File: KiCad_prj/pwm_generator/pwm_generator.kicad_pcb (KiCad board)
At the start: 2 copper layers, 100 x 46 mm, 89 parts, among them J1 MLW20A, J2 MLW10A, U1 LM2664 / LM2665, U10 OPA365xxDBV, U11 TLV3501AIDBV, U12 OPA365xxDBV, U13 TLV3501AIDBV, U2 74HC14, U3 TL431DBZ, U4 OPA365xxDBV, U5 TLV3501AIDBV, U6 OPA197xDBV, U7 OPA197xDBV, U8 OPA197xDBV, U9 OPA197xDBV

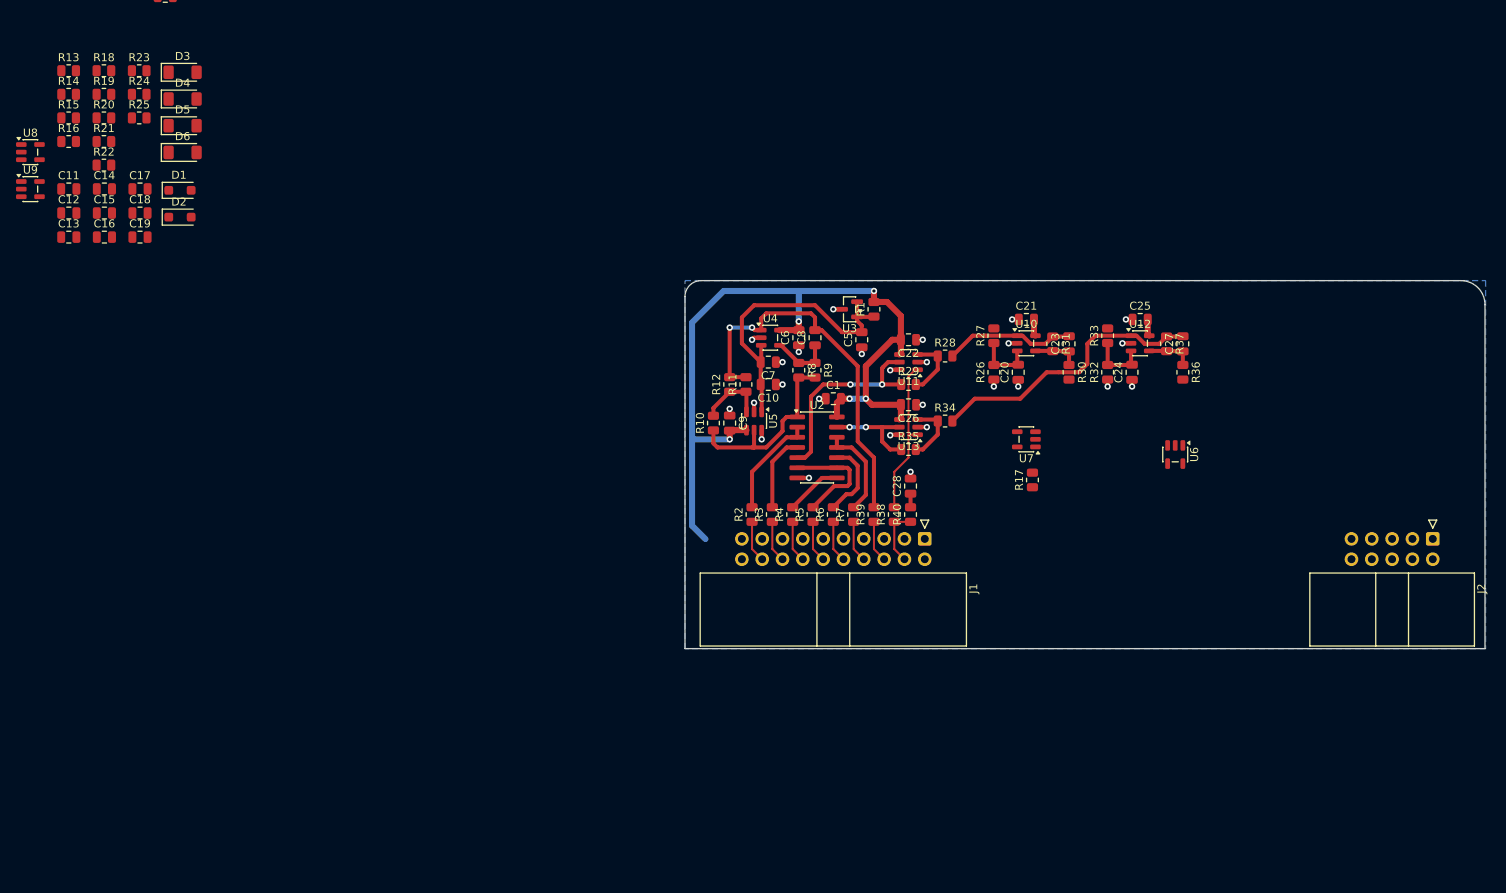
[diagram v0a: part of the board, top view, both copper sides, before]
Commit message: Upravaa DPS pwm generatoru
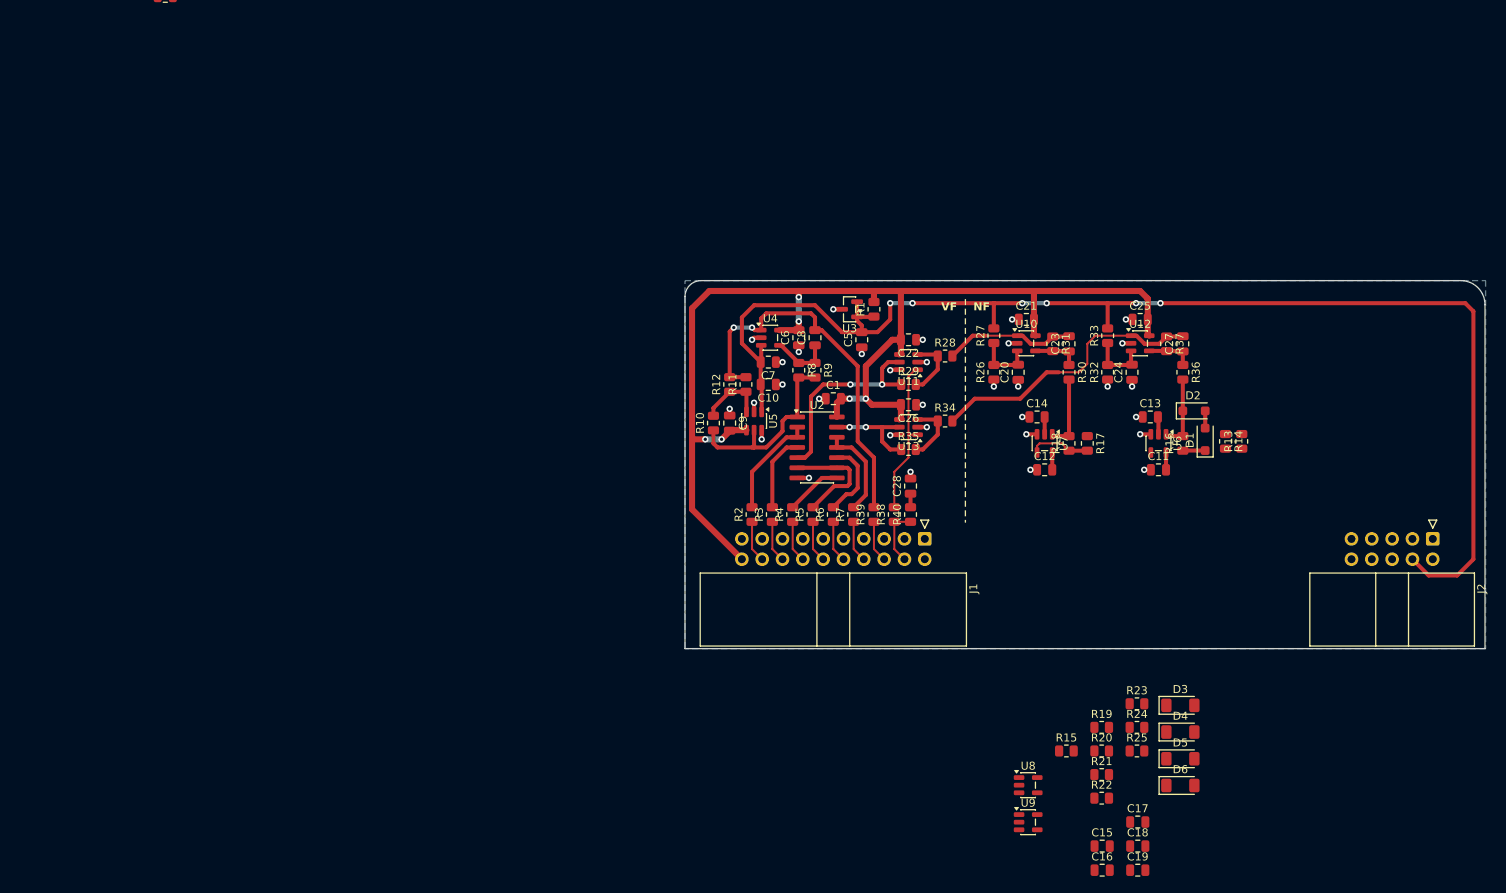
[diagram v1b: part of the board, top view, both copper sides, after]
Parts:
- moved R13 153.8 mm to (174.6, 104.1), turned to 90 degrees
- moved R14 151.0 mm to (172.6, 104.1), turned to -90 degrees
- moved C17 147.7 mm to (161.6, 151.7)
- moved C18 147.7 mm to (161.6, 154.7)
- moved C19 147.7 mm to (161.6, 157.7)
- moved R23 147.7 mm to (161.5, 136.9)
- moved R24 147.7 mm to (161.5, 139.8)
- moved R25 147.7 mm to (161.5, 142.8)
- moved C15 147.7 mm to (157.1, 154.7)
- moved C16 147.7 mm to (157.1, 157.7)
- moved D3 147.7 mm to (166.9, 137.1)
- moved D4 147.7 mm to (166.9, 140.4)
- moved D5 147.7 mm to (166.9, 143.8)
- moved D6 147.7 mm to (166.9, 147.1)
- moved R15 147.7 mm to (152.7, 142.8)
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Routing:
- net /U_{REF}: track 38.2 -> 164.3 mm, vias 0 -> 6
- net +5V: track 104.0 -> 153.0 mm, vias 5 -> 6
- net /PWM_CHA/SIGNAL_AC: track 0.00 -> 9.26 mm
- net /PWM_CHB/SIGNAL_AC: track 0.00 -> 9.26 mm
- net Net-(U7--): track 0.00 -> 7.61 mm
- net GND: track 25.5 -> 31.6 mm, vias 26 -> 32
- net -5V: track 0.00 -> 4.36 mm
- net Net-(D1-K): track 0.00 -> 2.80 mm
- net Net-(D1-A): track 0.00 -> 2.16 mm
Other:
- board text added: "NF"
- board text added: "VF"

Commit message: Dokoncene trasy na DPS pwm_generator
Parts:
- added C29: 100n, Capacitor_SMD:C_0805_2012Metric, F.Cu at (176.6, 91.9)
- added C30: 100n, Capacitor_SMD:C_0805_2012Metric, F.Cu at (142.6, 88.1)
- added C31: 100n, Capacitor_SMD:C_0805_2012Metric, F.Cu at (156.8, 88.1)
- added C32: 100n, Capacitor_SMD:C_0805_2012Metric, F.Cu at (109.6, 113.2)
- added C33: 100n, Capacitor_SMD:C_0805_2012Metric, F.Cu at (137.5, 113.2)
- moved C4 120.3 mm to (144.9, 107.4), turned to -90 degrees
- moved C3 119.9 mm to (141.6, 109.2)
- moved C2 117.8 mm to (138.3, 107.4), turned to -90 degrees
- moved U1 110.3 mm to (141.6, 106.4), turned to 180 degrees
- moved U3 47.7 mm to (173.1, 92.4), turned to -90 degrees
- moved R1 47.1 mm to (175.7, 89.1), turned to 0 degrees
- moved C19 45.7 mm to (148.9, 113.7)
- moved C5 44.5 mm to (171.5, 89.1), turned to 180 degrees
- moved C16 44.4 mm to (163.2, 113.7)
- moved R15 38.7 mm to (170.0, 108.2), turned to 90 degrees
- moved C18 36.3 mm to (150.0, 120.3)
- moved D4 35.9 mm to (142.3, 114.3), turned to 90 degrees
- moved C17 35.5 mm to (169.3, 117.0), turned to 90 degrees
- moved C15 35.0 mm to (164.2, 120.3)
- moved U9 34.7 mm to (150.0, 117.0), turned to -90 degrees
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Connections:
- J2 pad 10: /Wave Shaper/COMPENSATION_NEG -> /Wave Shaper/INPUT_SIGNAL
- J2 pad 2: /Wave Shaper/ACDC -> /U_{REF}
- J2 pad 4: /U_{REF} -> /Wave Shaper/ACDC
- J2 pad 6: /Wave Shaper/INPUT_SIGNAL -> /Wave Shaper/COMPENSATION_POS
- J2 pad 8: /Wave Shaper/COMPENSATION_POS -> /Wave Shaper/COMPENSATION_NEG
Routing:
- net +5V: track 153.0 -> 345.4 mm, vias 6 -> 16
- net -5V: track 4.36 -> 65.4 mm, vias 0 -> 4
- net /Wave Shaper/COMPENSATION_POS: track 0.00 -> 41.6 mm
- net /U_{REF}: track 164.3 -> 125.7 mm, vias 6 -> 0
- net /Wave Shaper/COMPENSATION_NEG: track 0.00 -> 28.0 mm
- net Net-(D5-A): track 0.00 -> 21.6 mm, vias 0 -> 2
- net /Wave Shaper/ACDC: track 0.00 -> 18.9 mm
- net /PWM_CHB/SIGNAL_AC: track 9.26 -> 26.3 mm
- net GND: track 31.6 -> 47.2 mm, vias 32 -> 47
- net Net-(D5-K): track 0.00 -> 11.9 mm
- net Net-(D3-A): track 0.00 -> 11.8 mm
- net Net-(C17-Pad2): track 0.00 -> 11.6 mm
- net /Wave Shaper/INPUT_SIGNAL: track 0.00 -> 10.1 mm
- net Net-(U8--): track 0.00 -> 9.32 mm
- net Net-(D1-K): track 2.80 -> 9.34 mm
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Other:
- board size 100 x 46 mm -> 90 x 46 mm
- board text removed: "NF"
- board text removed: "VF"

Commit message: Pruchozi kontrola DRC
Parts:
- moved C2 0.25 mm to (141.6, 109.4)
- renumbered C2 to C1, C7 to C10, C9 to C11, C6 to C12, C8 to C13, C10 to C14, C18 to C17, C19 to C18, C17 to C19, C3 to C2, C11 to C20, C13 to C21, C12 to C22, C14 to C23, C30 to C24, C20 to C25, C21 to C26, C23 to C27, C22 to C28, C31 to C29, C4 to C3, C24 to C30, C25 to C31, C27 to C32, C26 to C33, C29 to C4, C1 to C6, C28 to C7, C32 to C8, C33 to C9, D3 to D1, D4 to D2, D5 to D3, D6 to D4, D1 to D5, D2 to D6, J2 to J1, J1 to J2, R40 to R10, R8 to R11, R9 to R12, R10 to R13, R11 to R14, R12 to R15, R22 to R16, R24 to R17, R23 to R18, R20 to R19, R21 to R20, R25 to R21, R13 to R22, R14 to R23, R15 to R24, R19 to R25, R16 to R26, R17 to R27, R18 to R28, R27 to R29, R26 to R31, R31 to R32, R28 to R33, R29 to R34, R33 to R35, R32 to R37, R37 to R38, R34 to R39, R35 to R40, R39 to R8, R38 to R9, U3 to U2, U2 to U3, U5 to U4, U4 to U5, U8 to U6, U9 to U7, U6 to U8, U7 to U9
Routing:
- net Net-(D5-K): track 9.34 -> 14.7 mm
- net +5V: track 345.4 -> 347.9 mm
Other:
- board text added: "${TITLE} rev. ${REVISION}"
- board text added: "NF"
- board text added: "VF"

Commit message: Uprava DPS generatoru - popisky
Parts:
- added D7: LED, LED_SMD:LED_0805_2012Metric, F.Cu at (182.2, 91.9)
- added R41: 560R, Resistor_SMD:R_0805_2012Metric, F.Cu at (179.4, 90.9)
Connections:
- net /SAMP renamed /TRIG
- net /Triangle Wave Generator/~{SAMPLING} renamed /Triangle Wave Generator/~{TRIGGER}
- net /~{SAMP} renamed /~{TRIG}
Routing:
- net +5V: track 347.9 -> 306.1 mm
- net Net-(D7-A): track 0.00 -> 1.91 mm
- net GND: track 47.2 -> 48.1 mm, vias 47 -> 48
- added copper zone on F.Cu, net +5V
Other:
- board text added: "5V"
- board text added: "A"
- board text added: "AC"
- board text added: "B"
- board text added: "CN"
- board text added: "CP"
- board text added: "DC"
- board text added: "G"
- board text added: "IN"
- board text added: "POWER"
- board text added: "R"
- board text added: "TI"
- board text added: "TO"
- board text added: "TR"
- board text added: "~{A}"
- board text added: "~{B}"
- board text added: "~{TR}"

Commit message: Pridany testpointy a jlcpcb bom reference
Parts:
- added C34: 100n, Capacitor_SMD:C_0805_2012Metric, F.Cu at (174.6, 104.3)
- added R42: 1k, Resistor_SMD:R_0805_2012Metric, F.Cu at (176.6, 107.9)
- added TP1: TestPoint, TestPoint:TestPoint_Loop_D1.80mm_Drill1.0mm_Beaded, F.Cu at (130.4, 107.9)
- added TP2: TestPoint, TestPoint:TestPoint_Loop_D1.80mm_Drill1.0mm_Beaded, F.Cu at (129.4, 97.0)
- added TP3: TestPoint, TestPoint:TestPoint_Loop_D1.80mm_Drill1.0mm_Beaded, F.Cu at (128.7, 102.3)
- added TP4: TestPoint, TestPoint:TestPoint_Loop_D1.80mm_Drill1.0mm_Beaded, F.Cu at (190.9, 86.8)
- added TP5: TestPoint, TestPoint:TestPoint_Loop_D1.80mm_Drill1.0mm_Beaded, F.Cu at (178.5, 86.8)
- added TP6: TestPoint, TestPoint:TestPoint_Loop_D1.80mm_Drill1.0mm_Beaded, F.Cu at (172.4, 113.0)
- added TP7: TestPoint, TestPoint:TestPoint_Loop_D1.80mm_Drill1.0mm_Beaded, F.Cu at (141.1, 93.4)
- added TP8: TestPoint, TestPoint:TestPoint_Loop_D1.80mm_Drill1.0mm_Beaded, F.Cu at (141.1, 101.6)
- added TP9: TestPoint, TestPoint:TestPoint_Loop_D1.80mm_Drill1.0mm_Beaded, F.Cu at (153.0, 99.0)
- D1, D2, D3, D4: value LL4148 -> 1N4148WS; footprint Diode_SMD:D_MiniMELF -> Diode_SMD:D_SOD-323
- R10: value 100R -> 22R
- R22: value 2k5 -> 1k5
- moved R19 4.32 mm to (171.3, 117.0), turned to -90 degrees
- moved R22 2.03 mm to (176.6, 104.3)
- moved C5 1.14 mm to (170.4, 89.1), turned to -90 degrees
- moved D1 0.76 mm to (144.9, 115.0)
- moved D2 0.76 mm to (142.3, 115.0)
- moved D3 0.76 mm to (155.0, 117.0)
- moved D4 0.76 mm to (157.6, 117.0)
- moved C4 0.76 mm to (175.9, 91.9)
- moved R1 0.74 mm to (175.0, 89.1)
- moved C24 0.25 mm to (142.8, 88.1)
- moved R29 0.25 mm to (143.9, 90.9)
- moved R31 0.25 mm to (143.9, 95.5)
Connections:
- net /PWM_CHA/SIGNAL_AC renamed /SIGNAL_REF
- net /PWM_CHB/SIGNAL_AC renamed /~{SIGNAL_REF}
- net /Wave Shaper/INPUT_SIGNAL renamed /INPUT_SIGNAL
- net Net-(C27-Pad2) renamed /REF_CHA
- net Net-(C32-Pad2) renamed /REF_CHB
- R22 pad 1: /Wave Shaper/ACDC -> Net-(R22-Pad1)
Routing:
- net +5V: track 306.1 -> 311.2 mm
- net /Wave Shaper/ACDC: track 18.9 -> 15.9 mm
- net Net-(C34-Pad2): track 2.03 -> 4.10 mm
- net Net-(R22-Pad1): track 0.00 -> 1.73 mm
- net /TRIANGLE_OUT: track 46.8 -> 48.3 mm
- net /INPUT_SIGNAL: track 10.1 -> 11.5 mm
- net /TRIANGLE_IN: track 19.7 -> 20.8 mm
- net /U_{REF}: track 125.7 -> 124.6 mm
- net /REF_CHA: track 16.4 -> 17.3 mm
- net /PWM_CHB: track 12.4 -> 13.3 mm, vias 2 -> 1
- net Net-(D3-A): track 21.6 -> 22.4 mm
- net /PWM_CHA: track 25.3 -> 25.5 mm, vias 2 -> 1
- net GND: track 48.1 -> 48.0 mm, vias 48 -> 49
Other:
- board text removed: "POWER"

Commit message: Doplnene testovaci body a popisky
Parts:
- added TP11: U_{REF}, TestPoint:TestPoint_Loop_D1.80mm_Drill1.0mm_Beaded, F.Cu at (173.9, 97.0)
- added TP4: Trigger, TestPoint:TestPoint_Loop_D1.80mm_Drill1.0mm_Beaded, F.Cu at (113.4, 107.9)
- TP1: value TestPoint -> Triangle In
- TP10: renamed from TP8; value TestPoint -> Ref ChB
- TP2: value TestPoint -> PWM ChA
- TP3: value TestPoint -> PWM ChB
- TP5: value TestPoint -> SUP +5V
- TP6: renamed from TP4; value TestPoint -> SUP GND
- TP7: renamed from TP6; value TestPoint -> Signal In
- TP8: renamed from TP9; value TestPoint -> Signal Ref
- TP9: renamed from TP7; value TestPoint -> Ref ChA
- moved D1 1.27 mm to (183.0, 90.9), turned to 180 degrees
- moved TP1 0.25 mm to (130.4, 107.6)
- renumbered C34 to C20, C20 to C21, C21 to C22, C22 to C23, C23 to C24, C24 to C25, C25 to C26, C26 to C27, C27 to C28, C28 to C29, C29 to C30, C30 to C31, C31 to C32, C32 to C33, C33 to C34, D7 to D1, D1 to D2, D2 to D3, D3 to D4, D4 to D5, D5 to D6, D6 to D7, R9 to R10, R10 to R11, R11 to R12, R12 to R13, R13 to R14, R14 to R15, R15 to R16, R16 to R17, R17 to R18, R18 to R19, R41 to R2, R19 to R20, R42 to R21, R20 to R22, R21 to R23, R22 to R24, R23 to R25, R24 to R26, R25 to R27, R26 to R28, R27 to R29, R2 to R3, R28 to R30, R29 to R31, R30 to R32, R31 to R33, R32 to R34, R33 to R35, R34 to R36, R35 to R37, R36 to R38, R37 to R39, R3 to R4, R38 to R40, R39 to R41, R40 to R42, R4 to R5, R5 to R6, R6 to R7, R7 to R8, R8 to R9
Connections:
- net Net-(R2-Pad2) renamed /TRIGGER
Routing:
- net GND: track 48.0 -> 48.5 mm
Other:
- board text added: "${c4830822-0a8e-4866-acf2-6c6dd654ff02:REFERENCE}:${c4830822-0a8e-4866-acf2-6c6dd654ff02:VALUE} ${3c9ced08-20c9-4e22-bf8d-0cad56da0c4e:REFERENCE}:${3c9ced08-20c9-4e22-bf8d-0cad56da0c4e:VALUE} ${965caf23-03aa-4ecb-b893-2a7ca9c1ee26:REFERENCE}:${965caf23-03aa-4ecb-b893-2a7ca9c1ee26:VALUE} ${55c473b1-655e-4231-aef7-06f05cfc6df8:REFERENCE}:${55c473b1-655e-4231-aef7-06f05cfc6df8:VALUE} ${e4223aeb-98ae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"
